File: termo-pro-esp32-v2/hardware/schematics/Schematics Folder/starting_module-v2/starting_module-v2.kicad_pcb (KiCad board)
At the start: 2 copper layers, 120 x 65 mm, 21 parts, among them J1 Screw_Terminal_01x02, J2 Screw_Terminal_01x02, J3 Conn_01x08_Pin, K1 SANYOU_SRD_Form_C, Q1 PN2222A, SW1 SW_Push_LED, U2 ESP32-C3_SUPERMINI_TH

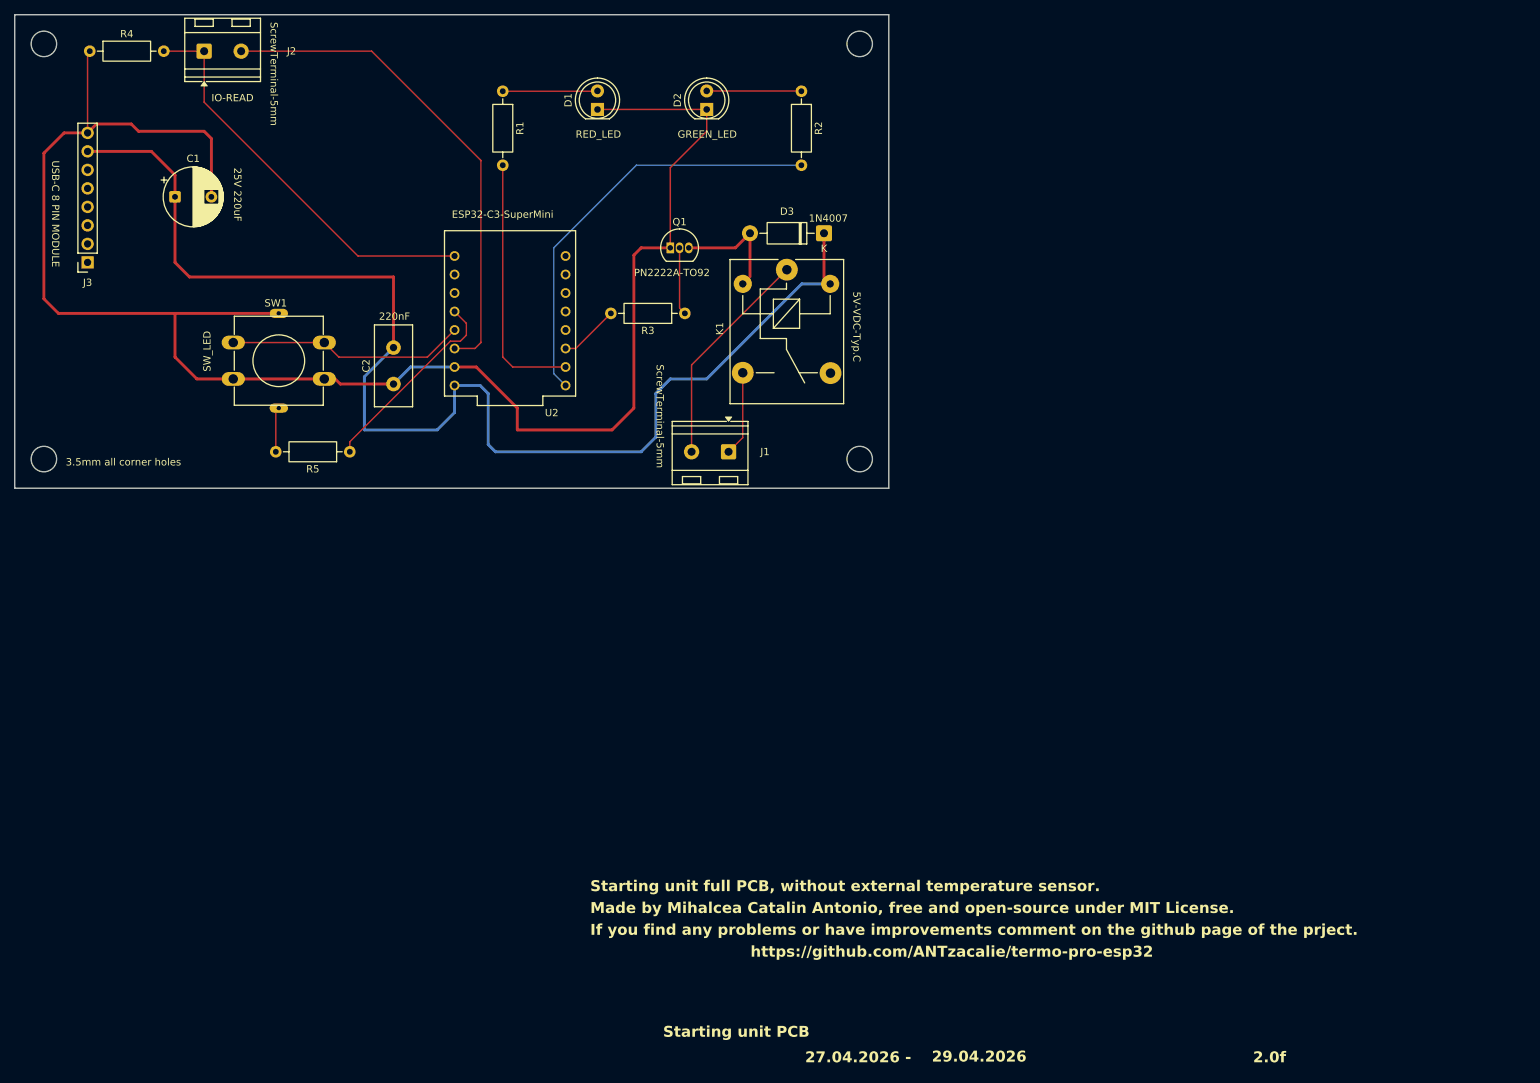
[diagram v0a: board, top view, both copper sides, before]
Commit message: Hardware part of the project is finished.
-DHT11 placement on thermostat unit fixed, pins trace redone.
-USB-C port on thermostat unit placed closer to edge by 4mm.
-Capacitors values recalculated and updated to closest common values, resistors values too.
-Starting unit pcb redone traces as relay and caps have been moved to the back plate.

-Starting & thermostat units PCB are done, inspected.
-Ready for fabrication.
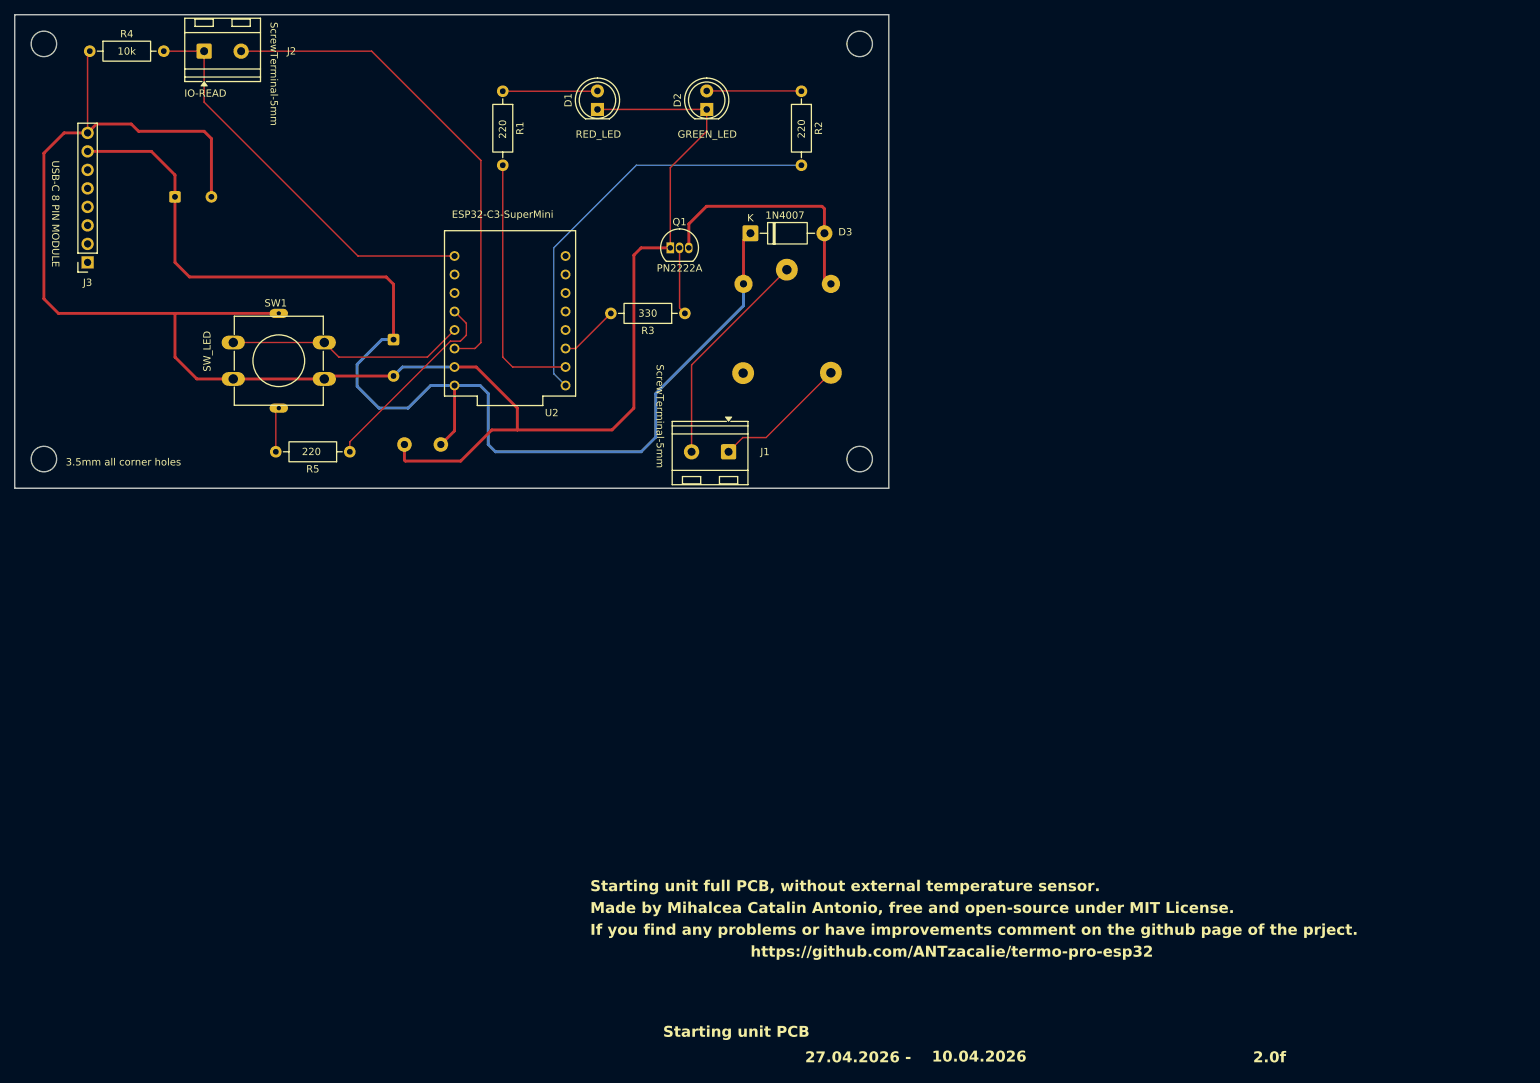
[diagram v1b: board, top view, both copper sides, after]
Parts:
- added C3: 10V 470uF, Capacitor_THT:CP_Radial_D8.0mm_P5.00mm, B.Cu at (152.0, 94.6)
- C1, C2, K1: moved to B.Cu
- R1, R2, R5: value 470 -> 220
- moved C2 10.5 mm to (158.5, 109.0), turned to 180 degrees
- moved D3 10.1 mm to (201.0, 80.0), turned to 0 degrees
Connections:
- C2 pad 1: GND -> /+VDC
- C2 pad 2: /+VDC -> GND
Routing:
- net GND: track 238.5 -> 258.9 mm
- net Net-(D3-A): track 16.6 -> 33.7 mm
- net /+VDC: track 175.7 -> 168.1 mm
- net Net-(J1-Pin_1): track 11.7 -> 18.5 mm
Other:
- board text added: "10.04.2026"
- board text added: "10V 470uF"
- board text added: "10k"
- board text added: "220"
- board text added: "330"
- board text removed: "220nF"
- board text removed: "29.04.2026"
- board text removed: "PN2222A-TO92"
